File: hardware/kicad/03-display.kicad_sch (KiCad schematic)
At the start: 2 parts, among them J4 FPC-16P-0.5mm

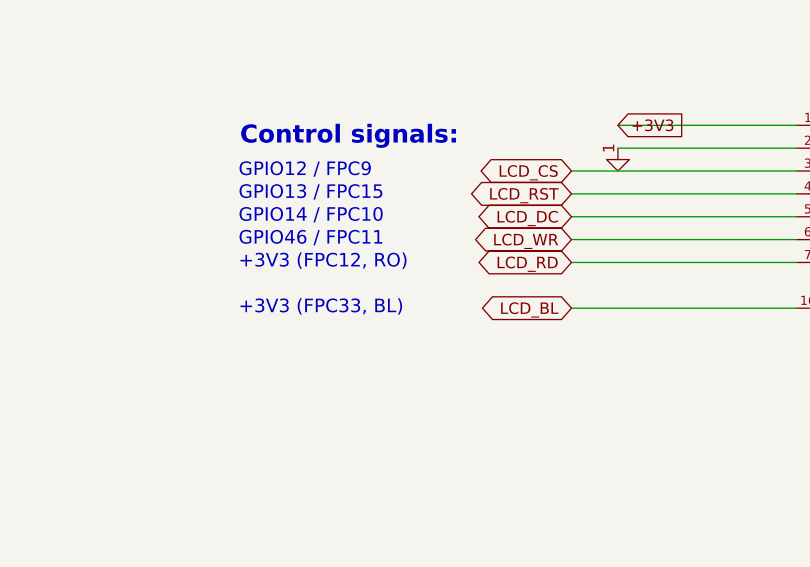
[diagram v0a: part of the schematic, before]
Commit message: triage: close the netlist disputes Phase 0 exposed — 29 down to 5
The plan forbids building the bench on a netlist in dispute, so the classes
scripts/vbench/netlist.py reported were worked through before Phase 1 opens.
Two of them were a fault in the detector, which is the more useful half.

D3 was a false-alarm class (17 -> 0). It reported every pad the schematic
translation table does not list and called them "compared by nothing". All
seventeen are declared in hardware/datasheet_specs.py, where
verify_datasheet_nets compares each against an expected net — 267 checks,
all passing. The four most suspicious readings dissolved on inspection:
U6.8/U6.9 on the SD data lines and SW_PWR.4b/4d on BTN_SELECT are
deliberate same-net assignments with a written safety analysis at
routing.py:6055-6085, protecting against real trace-through-pad shorts and
guarded by a hard gate. A check that fires on all seventeen discriminates
nothing, so D3 now fires only for a pad in NEITHER source — empty today,
and test_vbench injects one to prove the class still works, then requires
it to fall silent when the datasheet entry comes back.

Two of those entries were a real defect, in the table rather than the
board. _J1_MAP claimed "3,5,8 = SBU / unused, no net" and sent D+ to pad 6
and D- to pad 7 alone. The SBU pins are 3 and 9; pads 5 and 8 are the
flipped-orientation half of the pair and carry USB_D-/USB_D+, which
datasheet_specs.py::J1 states pad by pad citing USB-C r2.1 4.2. Two of the
four data pads were compared by nothing. T4 now compares all four.

The supply-rail stubs were the serious find. BAT+ had one node on the
schematic (SW_PWR.1) and VBUS had one (U4.5), because three local labels in
the Power Supply sheet sat 1.5-2 mm off the wires they name: VBUS at
vbus_y - 2, BAT+ at bat_y - 2, BAT_IN at jst_plus_y - 1.5. A label that
misses its wire leaves the wire unnamed, and KiCad drops unnamed nets from
the export — so the pins on them do not appear with a wrong net, they do
not ap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
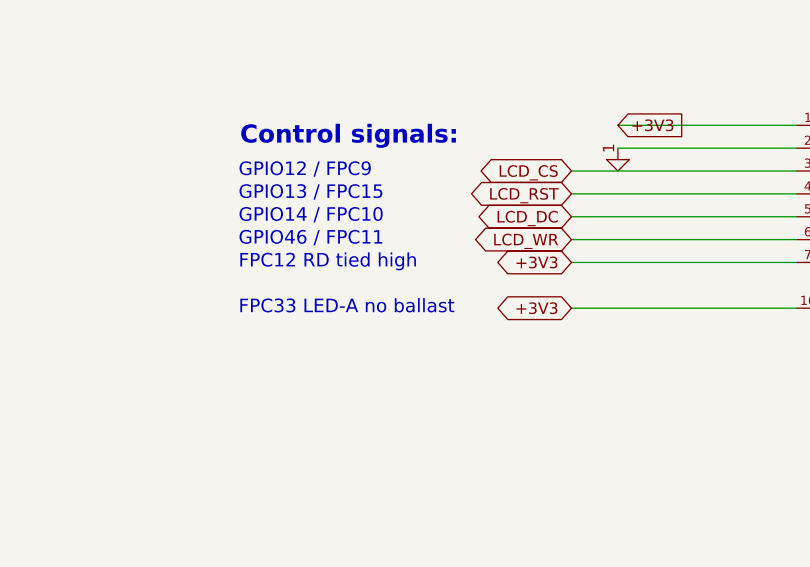
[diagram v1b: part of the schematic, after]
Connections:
- net LCD_BL is gone; now on net +3V3: DS1.16 (BL)
- net LCD_RD is gone; now on net +3V3: DS1.7 (RD)
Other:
- note added: "FPC12 RD tied high"
- note added: "FPC33 LED-A no ballast"
- note removed: "+3V3 (FPC12, RO)"
- note removed: "+3V3 (FPC33, BL)"
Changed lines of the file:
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@@
   (text "GPIO46 / FPC11" (at 75.84 117.46 0) (effects (font (size 1.5 1.5)) (justify left)))
   (wire (pts (xy 137.84 120) (xy 112.84 120)) (stroke (width 0) (type default)))
-  (global_label "LCD_RD" (shape bidirectional) (at 112.84 120 180) (effects (font (size 1.27 1.27))) (property "Intersheetrefs" "" (at 0 0 0) (effects (font (size 1.27 1.27)) hide)))
-  (text "+3V3 (FPC12, RO)" (at 75.84 120 0) (effects (font (size 1.5 1.5)) (justify left)))
+  (global_label "+3V3" (shape bidirectional) (at 112.84 120 180) (effects (font (size 1.27 1.27))) (property "Intersheetrefs" "" (at 0 0 0) (effects (font (size 1.27 1.27)) hide)))
+  (text "FPC12 RD tied high" (at 75.84 120 0) (effects (font (size 1.5 1.5)) (justify left)))
   (wire (pts (xy 137.84 125.08) (xy 112.84 125.08)) (stroke (width 0) (type default)))
-  (global_label "LCD_BL" (shape bidirectional) (at 112.84 125.08 180) (effects (font (size 1.27 1.27))) (property "Intersheetrefs" "" (at 0 0 0) (effects (font (size 1.27 1.27)) hide)))
-  (text "+3V3 (FPC33, BL)" (at 75.84 125.08 0) (effects (font (size 1.5 1.5)) (justify left)))
+  (global_label "+3V3" (shape bidirectional) (at 112.84 125.08 180) (effects (font (size 1.27 1.27))) (property "Intersheetrefs" "" (at 0 0 0) (effects (font (size 1.27 1.27)) hide)))
+  (text "FPC33 LED-A no ballast" (at 75.84 125.08 0) (effects (font (size 1.5 1.5)) (justify left)))
   (text "8-bit data bus:" (at 173 100 0) (effects (font (size 2 2) bold) (justify left)))
   (wire (pts (xy 158.16 104.76) (xy 183.16 104.76)) (stroke (width 0) (type default)))
